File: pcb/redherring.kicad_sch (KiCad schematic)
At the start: 192 parts, among them J2 OLED, SW3 Rotary_Encoder_Switch, U1 Elite-Pi

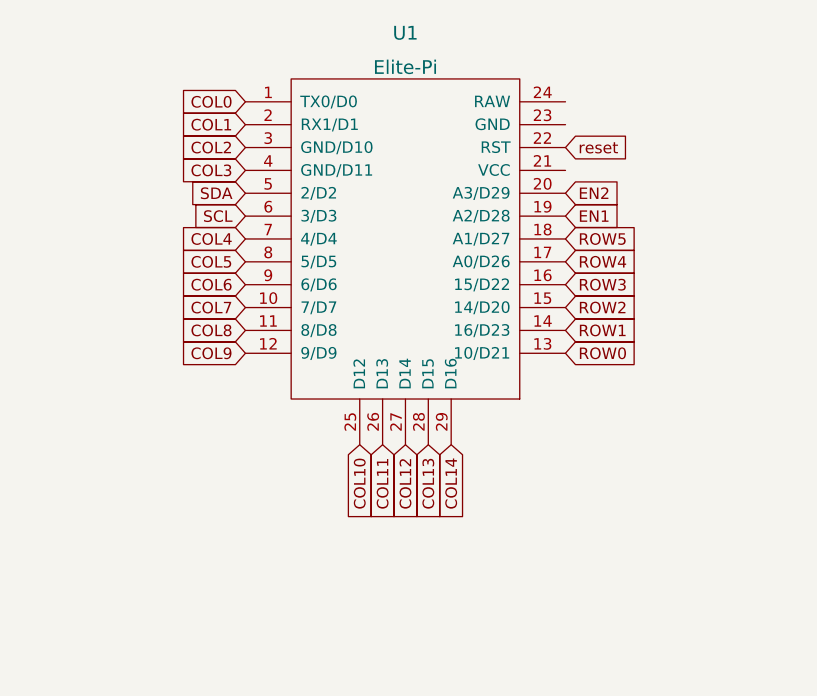
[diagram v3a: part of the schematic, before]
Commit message: Completed tracks for blueherring with elite-pi.
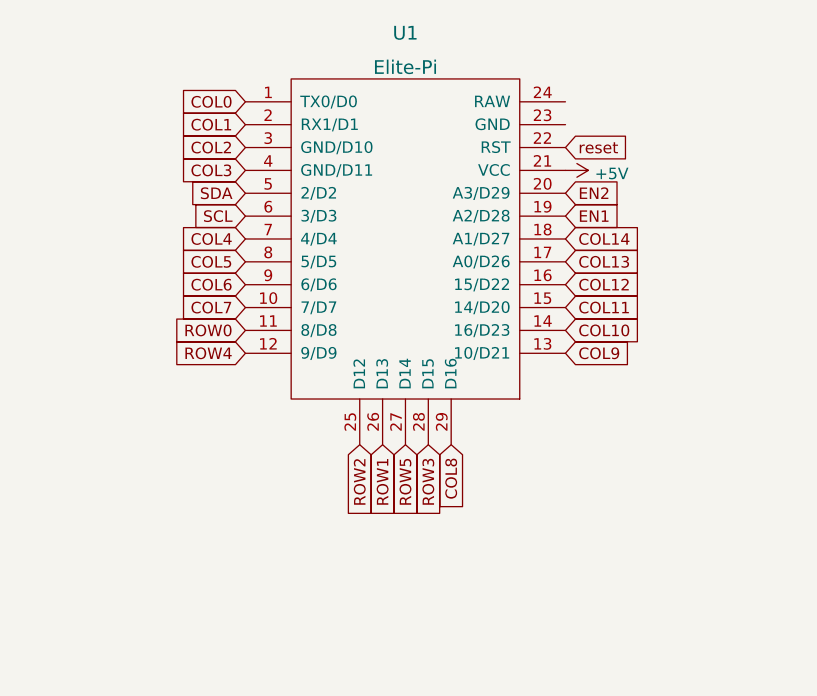
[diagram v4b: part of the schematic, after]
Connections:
- net +5V: now also U1.21 (VCC)
- net COL10: now also U1.14 (16/D23); no longer U1.25 (D12)
- net COL11: now also U1.15 (14/D20); no longer U1.26 (D13)
- net COL12: now also U1.16 (15/D22); no longer U1.27 (D14)
- net COL13: now also U1.17 (A0/D26); no longer U1.28 (D15)
- net COL14: now also U1.18 (A1/D27); no longer U1.29 (D16)
- net COL8: now also U1.29 (D16); no longer U1.11 (8/D8)
- net COL9: now also U1.13 (10/D21); no longer U1.12 (9/D9)
- net ROW0: now also U1.11 (8/D8); no longer U1.13 (10/D21)
- net ROW1: now also U1.26 (D13); no longer U1.14 (16/D23)
- net ROW2: now also U1.25 (D12); no longer U1.15 (14/D20)
- net ROW3: now also U1.28 (D15); no longer U1.16 (15/D22)
- net ROW4: now also U1.12 (9/D9); no longer U1.17 (A0/D26)
- net ROW5: now also U1.27 (D14); no longer U1.18 (A1/D27)
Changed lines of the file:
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@@
     )
   )
-  (global_label "ROW3" (shape input) (at 88.9 68.58 0) (fields_autoplaced)
+  (global_label "COL12" (shape input) (at 88.9 68.58 0) (fields_autoplaced)
     (effects (font (size 1.27 1.27)) (justify left))
-    (property "Intersheet References" "${INTERSHEET_REFS}" (id 0) (at 20.32 30.48 0)
-      (effects (font (size 1.27 1.27)) hide)
+    (property "Intersheet References" "${INTERSHEET_REFS}" (id 0) (at 97.2718 68.5006 0)
+      (effects (font (size 1.27 1.27)) (justify left) hide)
     )
   )
@@
     )
   )
-  (global_label "ROW2" (shape input) (at 88.9 71.12 0) (fields_autoplaced)
+  (global_label "COL11" (shape input) (at 88.9 71.12 0) (fields_autoplaced)
     (effects (font (size 1.27 1.27)) (justify left))
-    (property "Intersheet References" "${INTERSHEET_REFS}" (id 0) (at 20.32 25.4 0)
-      (effects (font (size 1.27 1.27)) hide)
+    (property "Intersheet References" "${INTERSHEET_REFS}" (id 0) (at 97.2718 71.0406 0)
+      (effects (font (size 1.27 1.27)) (justify left) hide)
     )
   )
@@
     )
   )
-  (global_label "COL13" (shape input) (at 73.66 86.36 270) (fields_autoplaced)
+  (global_label "ROW3" (shape input) (at 73.66 86.36 270) (fields_autoplaced)
     (effects (font (size 1.27 1.27)) (justify right))
-    (property "Intersheet References" "${INTERSHEET_REFS}" (id 0) (at 157.48 17.78 0)
-      (effects (font (size 1.27 1.27)) hide)
+    (property "Intersheet References" "${INTERSHEET_REFS}" (id 0) (at 73.5806 93.9456 90)
+      (effects (font (size 1.27 1.27)) (justify right) hide)
     )
   )
@@
     )
   )
-  (global_label "COL14" (shape input) (at 76.2 86.36 270) (fields_autoplaced)
+  (global_label "COL8" (shape input) (at 76.2 86.36 270) (fields_autoplaced)
     (effects (font (size 1.27 1.27)) (justify right))
-    (property "Intersheet References" "${INTERSHEET_REFS}" (id 0) (at 157.48 17.78 0)
-      (effects (font (size 1.27 1.27)) hide)
+    (property "Intersheet References" "${INTERSHEET_REFS}" (id 0) (at 76.1206 93.5223 90)
+      (effects (font (size 1.27 1.27)) (justify right) hide)
     )
   )
@@
     )
   )
-  (global_label "COL12" (shape input) (at 71.12 86.36 270) (fields_autoplaced)
+  (global_label "ROW5" (shape input) (at 71.12 86.36 270) (fields_autoplaced)
     (effects (font (size 1.27 1.27)) (justify right))
-    (property "Intersheet References" "${INTERSHEET_REFS}" (id 0) (at 157.48 17.78 0)
-      (effects (font (size 1.27 1.27)) hide)
+    (property "Intersheet References" "${INTERSHEET_REFS}" (id 0) (at 71.0406 93.9456 90)
+      (effects (font (size 1.27 1.27)) (justify right) hide)
     )
   )
@@
     )
   )
-  (global_label "ROW5" (shape input) (at 88.9 63.5 0) (fields_autoplaced)
+  (global_label "COL14" (shape input) (at 88.9 63.5 0) (fields_autoplaced)
     (effects (font (size 1.27 1.27)) (justify left))
-    (property "Intersheet References" "${INTERSHEET_REFS}" (id 0) (at 20.32 22.86 0)
-      (effects (font (size 1.27 1.27)) hide)
+    (property "Intersheet References" "${INTERSHEET_REFS}" (id 0) (at 97.2718 63.4206 0)
+      (effects (font (size 1.27 1.27)) (justify left) hide)
     )
   )
@@
     )
   )
-  (global_label "ROW0" (shape input) (at 88.9 76.2 0) (fields_autoplaced)
+  (global_label "COL9" (shape input) (at 88.9 76.2 0) (fields_autoplaced)
     (effects (font (size 1.27 1.27)) (justify left))
-    (property "Intersheet References" "${INTERSHEET_REFS}" (id 0) (at 20.32 -12.7 0)
-      (effects (font (size 1.27 1.27)) hide)
+    (property "Intersheet References" "${INTERSHEET_REFS}" (id 0) (at 96.0623 76.1206 0)
+      (effects (font (size 1.27 1.27)) (justify left) hide)
     )
   )
-  (global_label "COL9" (shape input) (at 53.34 76.2 180) (fields_autoplaced)
+  (global_label "ROW4" (shape input) (at 53.34 76.2 180) (fields_autoplaced)
     (effects (font (size 1.27 1.27)) (justify right))
-    (property "Intersheet References" "${INTERSHEET_REFS}" (id 0) (at 121.92 175.26 0)
-      (effects (font (size 1.27 1.27)) hide)
+    (property "Intersheet References" "${INTERSHEET_REFS}" (id 0) (at 45.7544 76.1206 0)
+      (effects (font (size 1.27 1.27)) (justify right) hide)
     )
   )
@@
     )
   )
-  (global_label "ROW4" (shape input) (at 88.9 66.04 0) (fields_autoplaced)
+  (global_label "COL13" (shape input) (at 88.9 66.04 0) (fields_autoplaced)
     (effects (font (size 1.27 1.27)) (justify left))
-    (property "Intersheet References" "${INTERSHEET_REFS}" (id 0) (at 20.32 -25.4 0)
-      (effects (font (size 1.27 1.27)) hide)
+    (property "Intersheet References" "${INTERSHEET_REFS}" (id 0) (at 97.2718 65.9606 0)
+      (effects (font (size 1.27 1.27)) (justify left) hide)
     )
   )
-  (global_label "ROW1" (shape input) (at 88.9 73.66 0) (fields_autoplaced)
+  (global_label "COL10" (shape input) (at 88.9 73.66 0) (fields_autoplaced)
     (effects (font (size 1.27 1.27)) (justify left))
-    (property "Intersheet References" "${INTERSHEET_REFS}" (id 0) (at 20.32 30.48 0)
-      (effects (font (size 1.27 1.27)) hide)
+    (property "Intersheet References" "${INTERSHEET_REFS}" (id 0) (at 97.2718 73.5806 0)
+      (effects (font (size 1.27 1.27)) (justify left) hide)
     )
   )
@@
     )
   )
-  (global_label "COL8" (shape input) (at 53.34 73.66 180) (fields_autoplaced)
+  (global_label "ROW0" (shape input) (at 53.34 73.66 180) (fields_autoplaced)
     (effects (font (size 1.27 1.27)) (justify right))
-    (property "Intersheet References" "${INTERSHEET_REFS}" (id 0) (at 121.92 170.18 0)
-      (effects (font (size 1.27 1.27)) hide)
+    (property "Intersheet References" "${INTERSHEET_REFS}" (id 0) (at 45.7544 73.5806 0)
+      (effects (font (size 1.27 1.27)) (justify right) hide)
     )
   )
@@
     )
   )
-  (global_label "COL11" (shape input) (at 68.58 86.36 270) (fields_autoplaced)
+  (global_label "ROW1" (shape input) (at 68.58 86.36 270) (fields_autoplaced)
     (effects (font (size 1.27 1.27)) (justify right))
-    (property "Intersheet References" "${INTERSHEET_REFS}" (id 0) (at 180.34 17.78 0)
-      (effects (font (size 1.27 1.27)) hide)
+    (property "Intersheet References" "${INTERSHEET_REFS}" (id 0) (at 68.5006 93.9456 90)
+      (effects (font (size 1.27 1.27)) (justify right) hide)
     )
   )
@@
     )
   )
-  (global_label "COL10" (shape input) (at 66.04 86.36 270) (fields_autoplaced)
+  (global_label "ROW2" (shape input) (at 66.04 86.36 270) (fields_autoplaced)
     (effects (font (size 1.27 1.27)) (justify right))
-    (property "Intersheet References" "${INTERSHEET_REFS}" (id 0) (at 175.26 17.78 0)
-      (effects (font (size 1.27 1.27)) hide)
+    (property "Intersheet References" "${INTERSHEET_REFS}" (id 0) (at 65.9606 93.9456 90)
+      (effects (font (size 1.27 1.27)) (justify right) hide)
     )
   )
@@
     (pin "2")
   )
+  (symbol (lib_id "power:+5V") (at 88.9 55.88 270) (unit 1)
+    (in_bom yes) (on_board yes)
+    (property "Reference" "#PWR?" (id 0) (at 85.09 55.88 0)
+      (effects (font (size 1.27 1.27)) hide)
+    )
+    (property "Value" "+5V" (id 1) (at 92.1512 56.261 90)
+      (effects (font (size 1.27 1.27)) (justify left))
+    )
+    (property "Footprint" "" (id 2) (at 88.9 55.88 0)
+      (effects (font (size 1.27 1.27)) hide)
+    )
+    (property "Datasheet" "" (id 3) (at 88.9 55.88 0)
+      (effects (font (size 1.27 1.27)) hide)
+    )
+    (pin "1")
+  )
   (symbol (lib_id "keebio:Elite-C") (at 71.12 62.23 0) (unit 1)
     (in_bom yes) (on_board yes) (fields_autoplaced)
@@
       (reference "#PWR0107") (unit 1) (value "GND") (footprint "")
     )
+    (path "/1843a80b-47fd-4052-bc50-3c13617b6571"
+      (reference "#PWR?") (unit 1) (value "+5V") (footprint "")
+    )
     (path "/00000000-0000-0000-0000-0000650e11f1"
